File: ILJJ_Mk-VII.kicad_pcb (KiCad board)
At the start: 2 copper layers, 48.3 x 99.1 mm, 28 parts, among them J1 Conn_02x12, U1 74LS00, U10 74LS00, U11 74LS00, U2 74LS00, U3 74LS00, U4 74LS00, U5 74LS00, U6 74LS00, U7 74LS00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

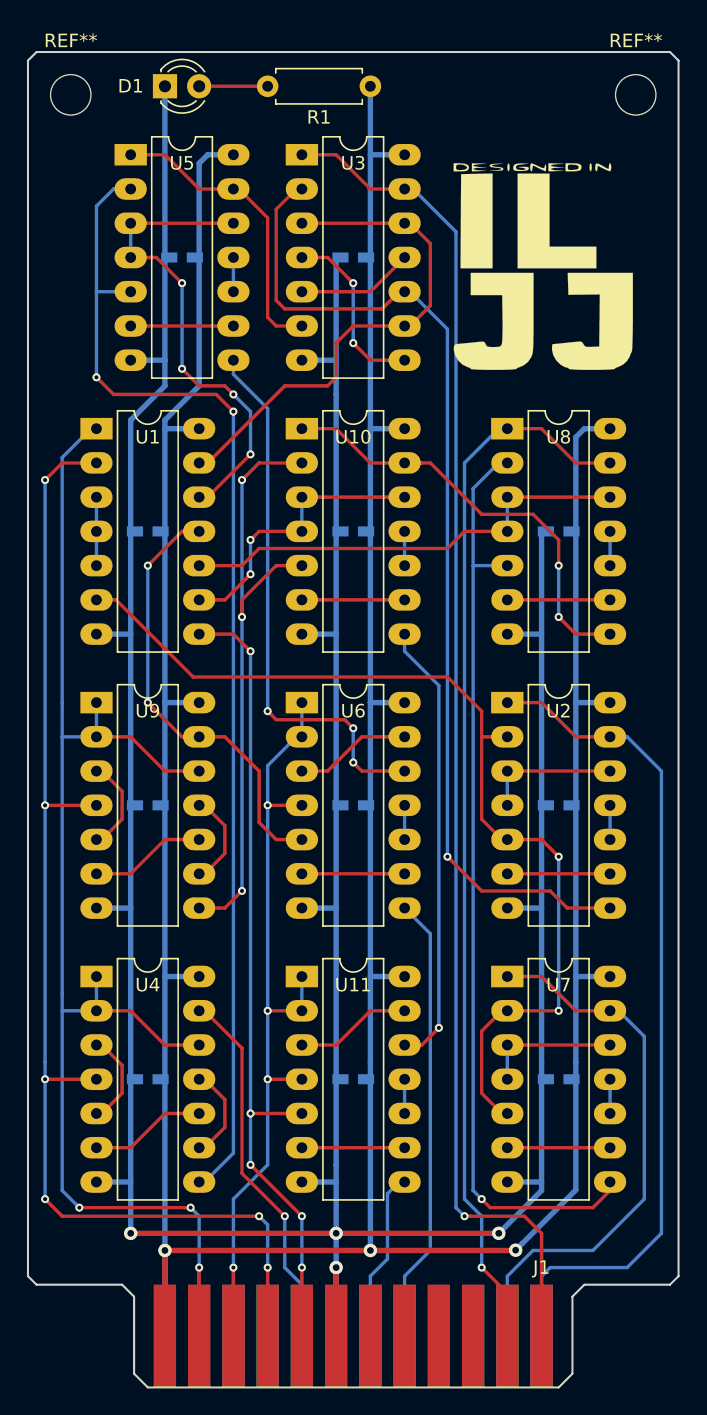
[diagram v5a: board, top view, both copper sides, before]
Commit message: [change] パワーランプの位置を変更
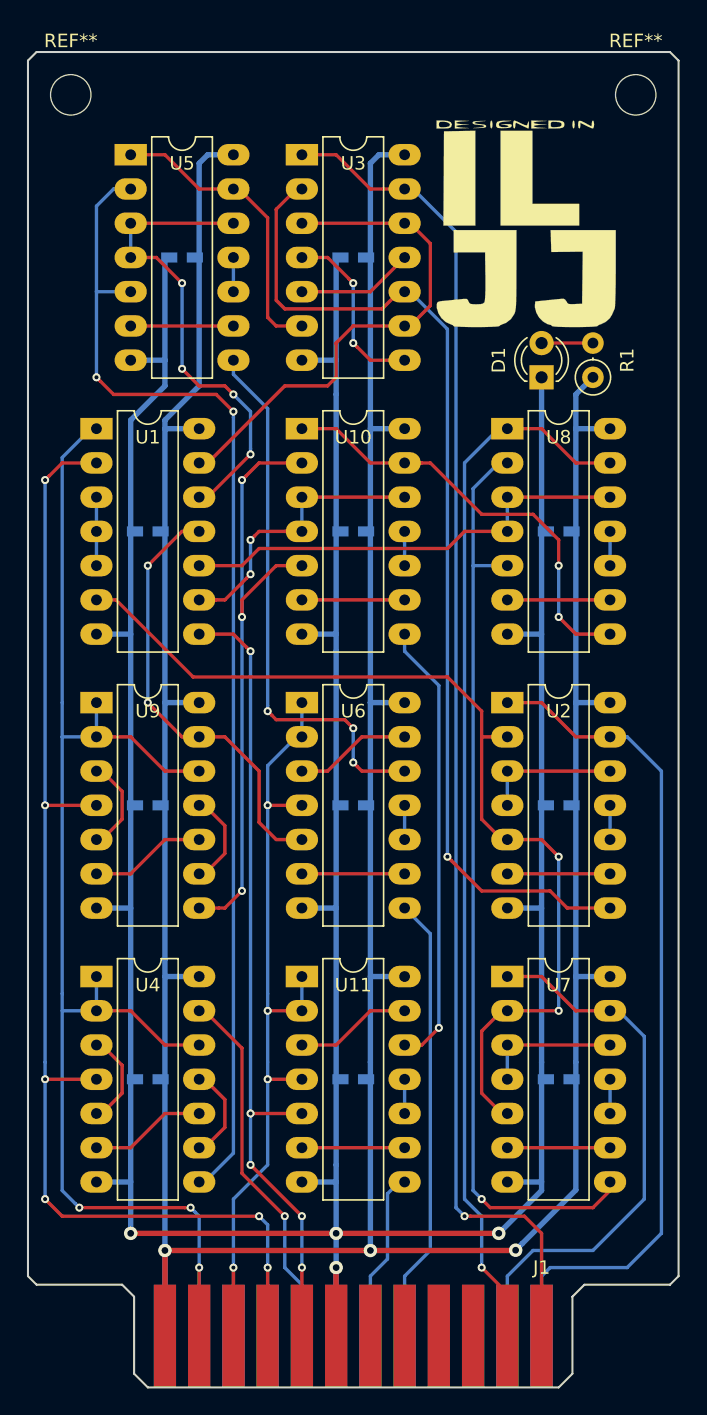
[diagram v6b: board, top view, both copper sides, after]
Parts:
- R1: footprint Resistors_ThroughHole:R_Axial_DIN0207_L6.3mm_D2.5mm_P7.62mm_Horizontal -> Resistors_ThroughHole:R_Axial_DIN0207_L6.3mm_D2.5mm_P2.54mm_Vertical
- moved D1 35.3 mm to (139.7, 74.9), turned to 90 degrees
- moved R1 27.2 mm to (143.5, 74.9), turned to 90 degrees
- moved G*** 3.42 mm to (138.4, 63.5)
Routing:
- net Net-(D1-Pad2): track 5.08 -> 3.81 mm
- net GND: track 282.7 -> 281.5 mm
- net VCC: track 300.9 -> 300.2 mm
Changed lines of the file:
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@@
     (thickness 1.6)
     (drawings 16)
-    (tracks 479)
+    (tracks 481)
     (zones 0)
     (modules 28)
@@
   )
   (module fplib:designed-in-ILJJ-small (layer F.Cu)
-    (at 139.7 66.675)
+    (at 138.43 63.5)
     (fp_text reference G*** (at 0 0) (layer F.SilkS) hide
       (effects (font (size 1.524 1.524) (thickness 0.3)))
@@
   )
   (module LEDs:LED_D3.0mm (layer F.Cu)
-    (at 111.76 53.34)
+    (at 139.7 74.93 90)
     (descr "LED, diameter 3.0mm, 2 pins")
     (tags "LED diameter 3.0mm 2 pins")
-    (fp_text reference D1 (at -2.54 0) (layer F.SilkS)
-      (effects (font (size 1 1) (thickness 0.15)))
-    )
-    (fp_text value POWER (at 1.27 2.96) (layer F.Fab)
+    (fp_text reference D1 (at 1.27 -3.175 90) (layer F.SilkS)
+      (effects (font (size 1 1) (thickness 0.15)))
+    )
+    (fp_text value POWER (at 1.27 2.96 90) (layer F.Fab)
       (effects (font (size 1 1) (thickness 0.15)))
     )
@@
     (fp_arc (start 1.27 0) (end -0.29 -1.235516) (angle 108.8) (layer F.SilkS) (width 0.12))
     (fp_arc (start 1.27 0) (end -0.23 -1.16619) (angle 284.3) (layer F.Fab) (width 0.1))
-    (pad 2 thru_hole circle (at 2.54 0) (size 1.8 1.8) (drill 0.9) (layers *.Cu *.Mask)
+    (pad 2 thru_hole circle (at 2.54 0 90) (size 1.8 1.8) (drill 0.9) (layers *.Cu *.Mask)
       (net 3 "Net-(D1-Pad2)"))
-    (pad 1 thru_hole rect (at 0 0) (size 1.8 1.8) (drill 0.9) (layers *.Cu *.Mask)
+    (pad 1 thru_hole rect (at 0 0 90) (size 1.8 1.8) (drill 0.9) (layers *.Cu *.Mask)
       (net 1 GND))
     (model ${KISYS3DMOD}/LEDs.3dshapes/LED_D3.0mm.wrl
@@
     (pad 24 connect rect (at 13.97 0) (size 1.651 7.62) (layers B.Cu B.Mask)
       (net 20 /B0))
-  )
-  (module Resistors_ThroughHole:R_Axial_DIN0207_L6.3mm_D2.5mm_P7.62mm_Horizontal (layer F.Cu)
-    (at 127 53.34 180)
-    (descr "Resistor, Axial_DIN0207 series, Axial, Horizontal, pin pitch=7.62mm, 0.25W = 1/4W, length*diameter=6.3*2.5mm^2, http://cdn-reichelt.de/documents/datenblatt/B400/1_4W%23YAG.pdf")
-    (tags "Resistor Axial_DIN0207 series Axial Horizontal pin pitch 7.62mm 0.25W = 1/4W length 6.3mm diameter 2.5mm")
-    (fp_text reference R1 (at 3.81 -2.31 180) (layer F.SilkS)
-      (effects (font (size 1 1) (thickness 0.15)))
-    )
-    (fp_text value R (at 3.81 2.31 180) (layer F.Fab)
-      (effects (font (size 1 1) (thickness 0.15)))
-    )
-    (fp_line (start 8.7 -1.6) (end -1.05 -1.6) (layer F.CrtYd) (width 0.05))
-    (fp_line (start 8.7 1.6) (end 8.7 -1.6) (layer F.CrtYd) (width 0.05))
-    (fp_line (start -1.05 1.6) (end 8.7 1.6) (layer F.CrtYd) (width 0.05))
-    (fp_line (start -1.05 -1.6) (end -1.05 1.6) (layer F.CrtYd) (width 0.05))
-    (fp_line (start 7.02 1.31) (end 7.02 0.98) (layer F.SilkS) (width 0.12))
-    (fp_line (start 0.6 1.31) (end 7.02 1.31) (layer F.SilkS) (width 0.12))
-    (fp_line (start 0.6 0.98) (end 0.6 1.31) (layer F.SilkS) (width 0.12))
-    (fp_line (start 7.02 -1.31) (end 7.02 -0.98) (layer F.SilkS) (width 0.12))
-    (fp_line (start 0.6 -1.31) (end 7.02 -1.31) (layer F.SilkS) (width 0.12))
-    (fp_line (start 0.6 -0.98) (end 0.6 -1.31) (layer F.SilkS) (width 0.12))
-    (fp_line (start 7.62 0) (end 6.96 0) (layer F.Fab) (width 0.1))
-    (fp_line (start 0 0) (end 0.66 0) (layer F.Fab) (width 0.1))
-    (fp_line (start 6.96 -1.25) (end 0.66 -1.25) (layer F.Fab) (width 0.1))
-    (fp_line (start 6.96 1.25) (end 6.96 -1.25) (layer F.Fab) (width 0.1))
-    (fp_line (start 0.66 1.25) (end 6.96 1.25) (layer F.Fab) (width 0.1))
-    (fp_line (start 0.66 -1.25) (end 0.66 1.25) (layer F.Fab) (width 0.1))
-    (pad 2 thru_hole oval (at 7.62 0 180) (size 1.6 1.6) (drill 0.8) (layers *.Cu *.Mask)
-      (net 3 "Net-(D1-Pad2)"))
-    (pad 1 thru_hole circle (at 0 0 180) (size 1.6 1.6) (drill 0.8) (layers *.Cu *.Mask)
-      (net 2 VCC))
-    (model ${KISYS3DMOD}/Resistors_THT.3dshapes/R_Axial_DIN0207_L6.3mm_D2.5mm_P7.62mm_Horizontal.wrl
-      (at (xyz 0 0 0))
-      (scale (xyz 0.393701 0.393701 0.393701))
-      (rotate (xyz 0 0 0))
-    )
   )
   (module Housings_DIP:DIP-14_W7.62mm_LongPads (layer F.Cu)
@@
     (fp_circle (center 0 0) (end 3.25 0) (layer F.CrtYd) (width 0.05))
     (pad 1 np_thru_hole circle (at 0 0) (size 3 3) (drill 3) (layers *.Cu *.Mask))
+  )
+  (module Resistors_ThroughHole:R_Axial_DIN0207_L6.3mm_D2.5mm_P2.54mm_Vertical (layer F.Cu)
+    (at 143.51 74.93 90)
+    (descr "Resistor, Axial_DIN0207 series, Axial, Vertical, pin pitch=2.54mm, 0.25W = 1/4W, length*diameter=6.3*2.5mm^2, http://cdn-reichelt.de/documents/datenblatt/B400/1_4W%23YAG.pdf")
+    (tags "Resistor Axial_DIN0207 series Axial Vertical pin pitch 2.54mm 0.25W = 1/4W length 6.3mm diameter 2.5mm")
+    (fp_text reference R1 (at 1.27 2.54 90) (layer F.SilkS)
+      (effects (font (size 1 1) (thickness 0.15)))
+    )
+    (fp_text value R (at 1.27 -1.905 90) (layer F.Fab)
+      (effects (font (size 1 1) (thickness 0.15)))
+    )
+    (fp_line (start 3.65 -1.6) (end -1.6 -1.6) (layer F.CrtYd) (width 0.05))
+    (fp_line (start 3.65 1.6) (end 3.65 -1.6) (layer F.CrtYd) (width 0.05))
+    (fp_line (start -1.6 1.6) (end 3.65 1.6) (layer F.CrtYd) (width 0.05))
+    (fp_line (start -1.6 -1.6) (end -1.6 1.6) (layer F.CrtYd) (width 0.05))
+    (fp_line (start 1.31 0) (end 1.44 0) (layer F.SilkS) (width 0.12))
+    (fp_line (start 0 0) (end 2.54 0) (layer F.Fab) (width 0.1))
+    (fp_circle (center 0 0) (end 1.31 0) (layer F.SilkS) (width 0.12))
+    (fp_circle (center 0 0) (end 1.25 0) (layer F.Fab) (width 0.1))
+    (pad 2 thru_hole oval (at 2.54 0 90) (size 1.6 1.6) (drill 0.8) (layers *.Cu *.Mask)
+      (net 3 "Net-(D1-Pad2)"))
+    (pad 1 thru_hole circle (at 0 0 90) (size 1.6 1.6) (drill 0.8) (layers *.Cu *.Mask)
+      (net 2 VCC))
+    (model ${KISYS3DMOD}/Resistors_THT.3dshapes/R_Axial_DIN0207_L6.3mm_D2.5mm_P2.54mm_Vertical.wrl
+      (at (xyz 0 0 0))
+      (scale (xyz 0.393701 0.393701 0.393701))
+      (rotate (xyz 0 0 0))
+    )
   )
   (gr_line (start 141.986 143.129) (end 142.875 142.24) (layer Edge.Cuts) (width 0.15))
@@
   (segment (start 139.7 135.255) (end 139.7 125.73) (width 0.4) (layer B.Cu) (net 1))
   (segment (start 136.525 138.43) (end 139.7 135.255) (width 0.4) (layer B.Cu) (net 1))
-  (segment (start 111.76 73.66) (end 111.76 53.34) (width 0.4) (layer B.Cu) (net 1))
+  (segment (start 111.76 73.66) (end 111.76 66.04) (width 0.4) (layer B.Cu) (net 1))
+  (segment (start 139.7 74.93) (end 139.7 86.36) (width 0.4) (layer B.Cu) (net 1))
   (segment (start 111.76 119.38) (end 114.3 119.38) (width 0.4) (layer B.Cu) (net 2))
   (segment (start 111.76 99.06) (end 114.3 99.06) (width 0.4) (layer B.Cu) (net 2))
   (segment (start 111.76 99.06) (end 111.76 118.11) (width 0.4) (layer B.Cu) (net 2))
-  (segment (start 129.54 58.42) (end 127 58.42) (width 0.4) (layer B.Cu) (net 2))
   (segment (start 127 119.38) (end 129.54 119.38) (width 0.4) (layer B.Cu) (net 2))
   (segment (start 127 99.06) (end 129.54 99.06) (width 0.4) (layer B.Cu) (net 2))
@@
   (segment (start 114.3 75.565) (end 114.3 59.055) (width 0.4) (layer B.Cu) (net 2))
   (segment (start 111.76 78.74) (end 111.76 78.105) (width 0.4) (layer B.Cu) (net 2))
-  (segment (start 142.875 78.74) (end 144.78 78.74) (width 0.4) (layer B.Cu) (net 2))
-  (segment (start 142.24 79.375) (end 142.875 78.74) (width 0.4) (layer B.Cu) (net 2))
-  (segment (start 142.24 99.06) (end 142.24 79.375) (width 0.4) (layer B.Cu) (net 2))
-  (segment (start 127 60.96) (end 127 53.34) (width 0.4) (layer B.Cu) (net 2))
-  (segment (start 127 99.06) (end 127 60.96) (width 0.4) (layer B.Cu) (net 2))
-  (segment (start 119.38 53.34) (end 114.3 53.34) (width 0.25) (layer F.Cu) (net 3))
+  (segment (start 127 59.055) (end 127 99.06) (width 0.4) (layer B.Cu) (net 2))
+  (segment (start 127.635 58.42) (end 127 59.055) (width 0.4) (layer B.Cu) (net 2))
+  (segment (start 129.54 58.42) (end 127.635 58.42) (width 0.4) (layer B.Cu) (net 2))
+  (segment (start 142.24 78.74) (end 144.78 78.74) (width 0.4) (layer B.Cu) (net 2))
+  (segment (start 142.24 99.06) (end 142.24 78.74) (width 0.4) (layer B.Cu) (net 2))
+  (segment (start 142.24 76.2) (end 143.51 74.93) (width 0.4) (layer B.Cu) (net 2))
+  (segment (start 142.24 78.74) (end 142.24 76.2) (width 0.4) (layer B.Cu) (net 2))
+  (segment (start 139.7 72.39) (end 143.51 72.39) (width 0.25) (layer F.Cu) (net 3))
   (segment (start 106.68 121.92) (end 109.22 121.92) (width 0.25) (layer F.Cu) (net 4))
   (segment (start 111.76 124.46) (end 114.3 124.46) (width 0.25) (layer F.Cu) (net 4))

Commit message: [add] board info
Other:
- board text added: "ILJJ Mk-VIIa 2bit ALU Card"
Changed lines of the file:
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@@
   (general
     (thickness 1.6)
-    (drawings 16)
+    (drawings 17)
     (tracks 481)
     (zones 0)
@@
     )
   )
+  (gr_text "ILJJ Mk-VIIa\n2bit ALU Card\n" (at 119.38 53.975) (layer F.SilkS)
+    (effects (font (size 1.2 1.2) (thickness 0.24)))
+  )
   (gr_line (start 141.986 143.129) (end 142.875 142.24) (layer Edge.Cuts) (width 0.15))
